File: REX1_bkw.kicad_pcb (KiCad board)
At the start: 2 copper layers, 16 x 38 mm, 10 parts, among them J1 Molex_DIP28_edge_contacts, J2 JTAG, J3 PRG, U1 XCR3064XL-10VQ44, U2 29F800, U3 LP2980

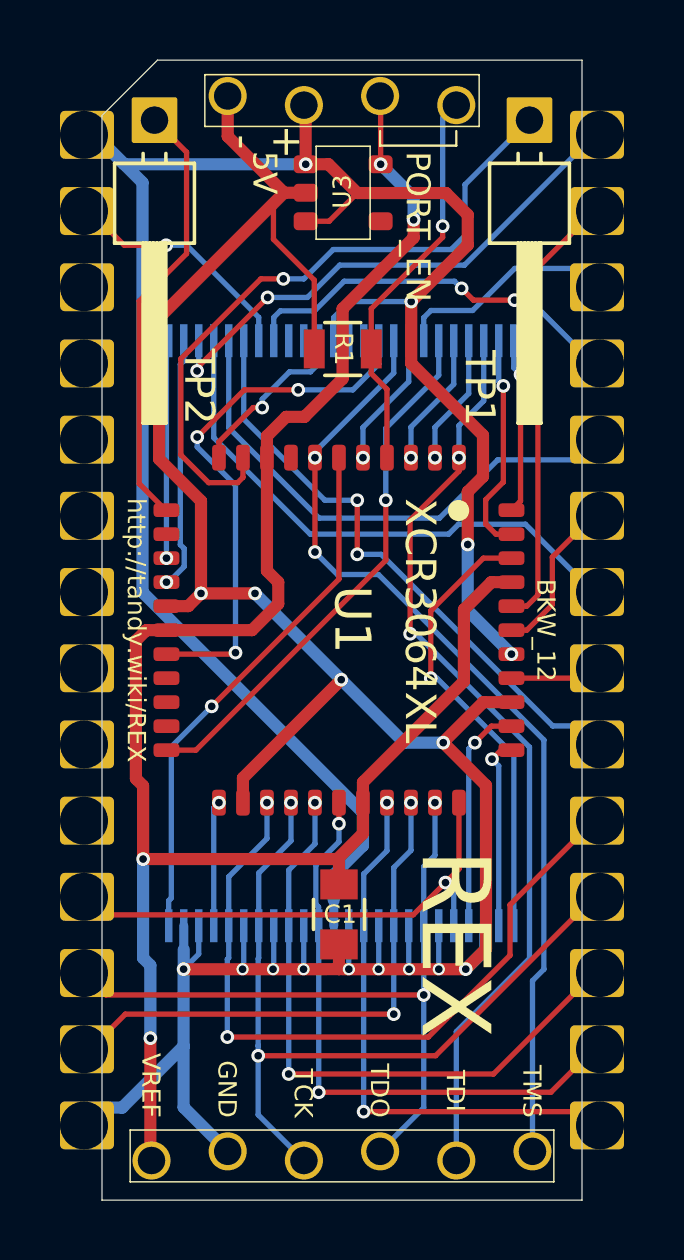
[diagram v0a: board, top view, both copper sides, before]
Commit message: update to latest pcb2molex8878 carrier and pcb outline
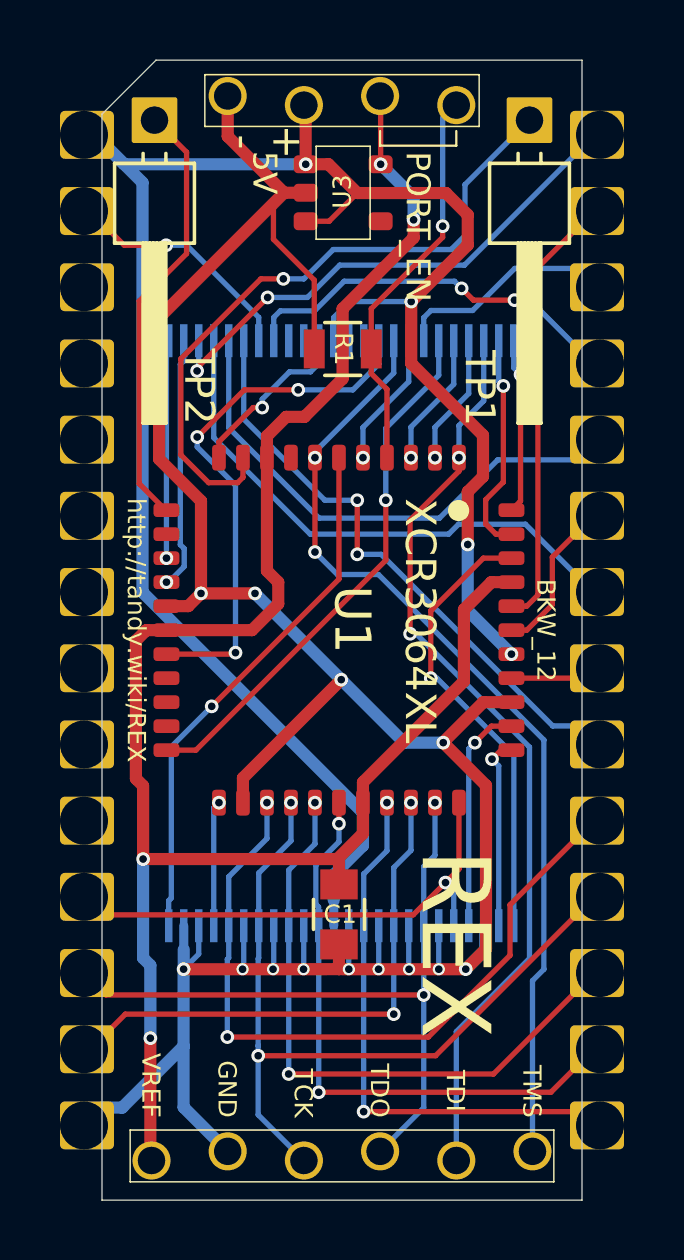
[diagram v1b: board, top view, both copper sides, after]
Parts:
- added carrier?: pcb2molex8878_chamfer, 000_LOCAL:pcb2molex8878_chamfer, F.Cu at (147.2, 99.2)
- J1: footprint 000_LOCAL:pcb2molex8878_chamfer -> 000_LOCAL:pcb2molex8878
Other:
- outline, holes or cut-outs redrawn
